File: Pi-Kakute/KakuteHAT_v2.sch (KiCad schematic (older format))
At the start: 51 parts, among them J1 40HAT, J12 FC_Socket, J2 Conn_01x02, J3 I2C, J4 Mout1_2, J5 Mout3_4, J6 RC_IN, J7 GPS2, J8 Power_Pad, J9 FC_Socket2, Q1 DMMT5401, Q2 DMG2305UX, SW1 Pi Power Switch, SW2 Pi Power Switch, U1 TPS22810, U2 AP2204RA-3.3, U3 KakuteF4_V2, U4 TPS54331DR, U5 NC7SZ00P5X, U6 CAT24C32

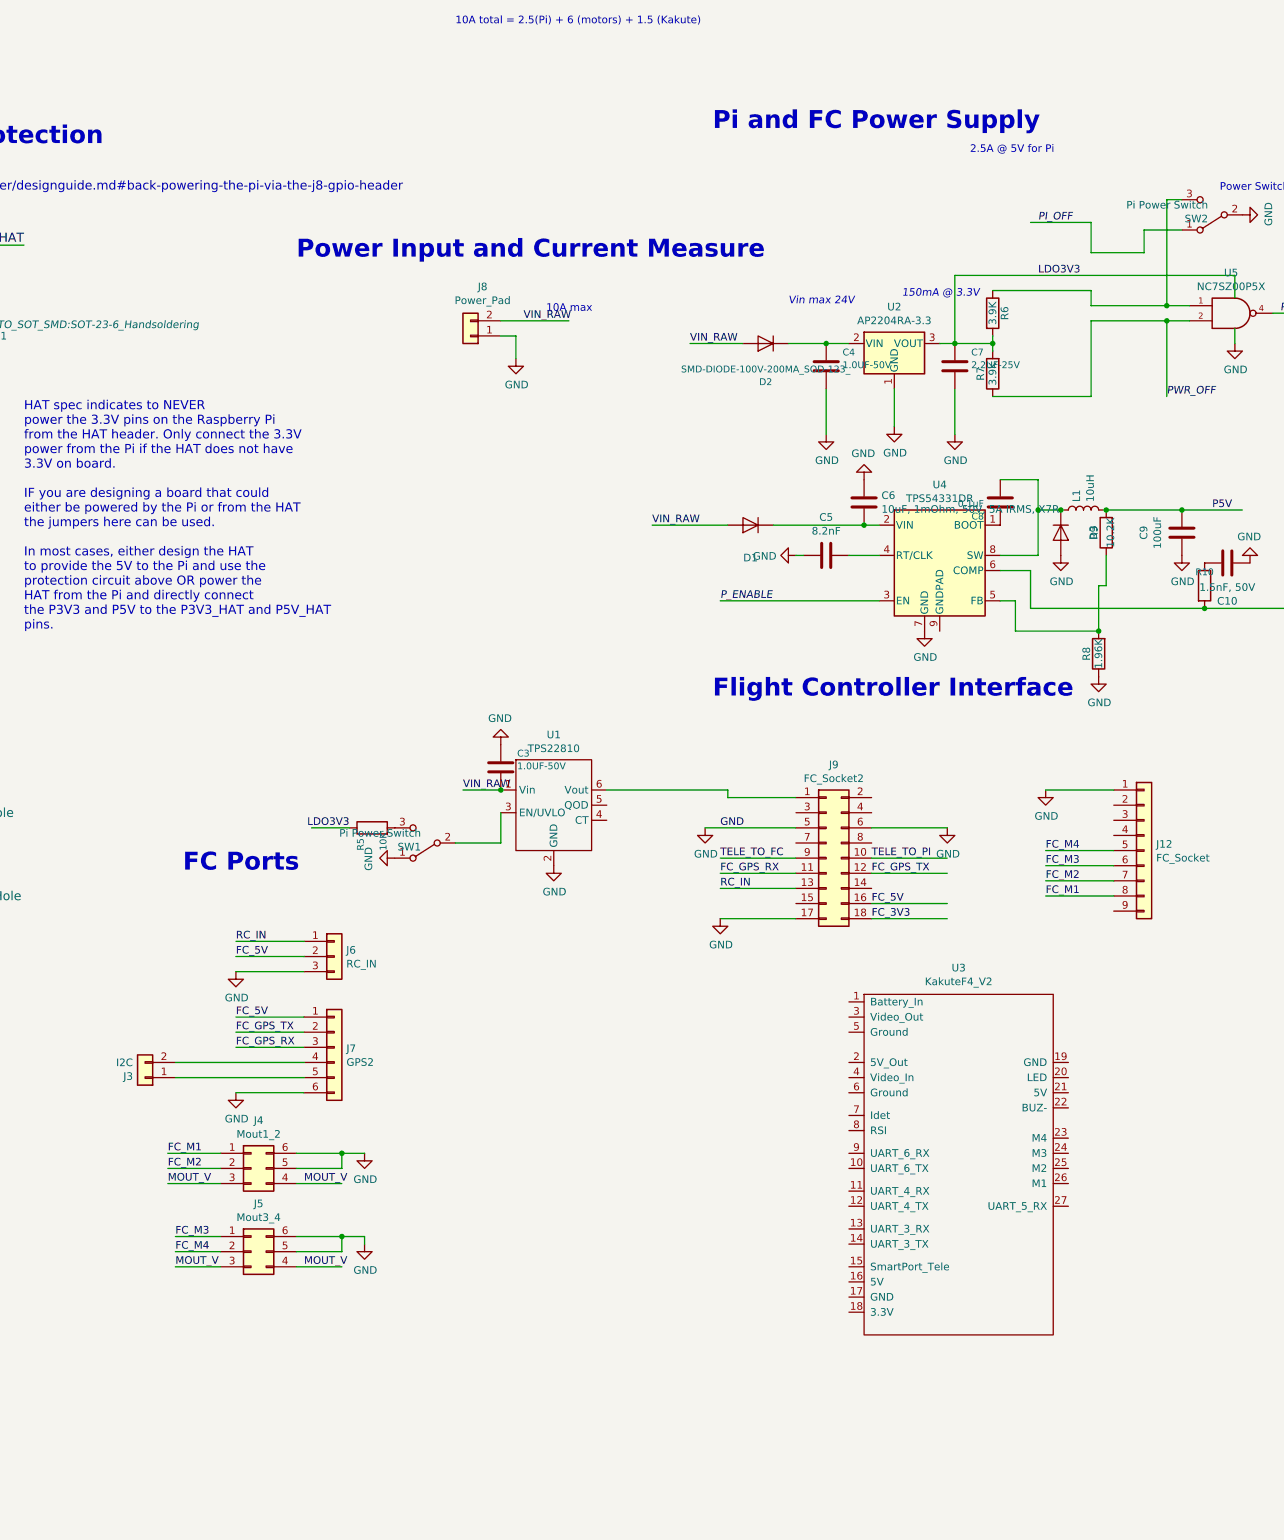
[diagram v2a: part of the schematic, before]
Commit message: Pi-Kakute: Updated power input to match Pi-Connect
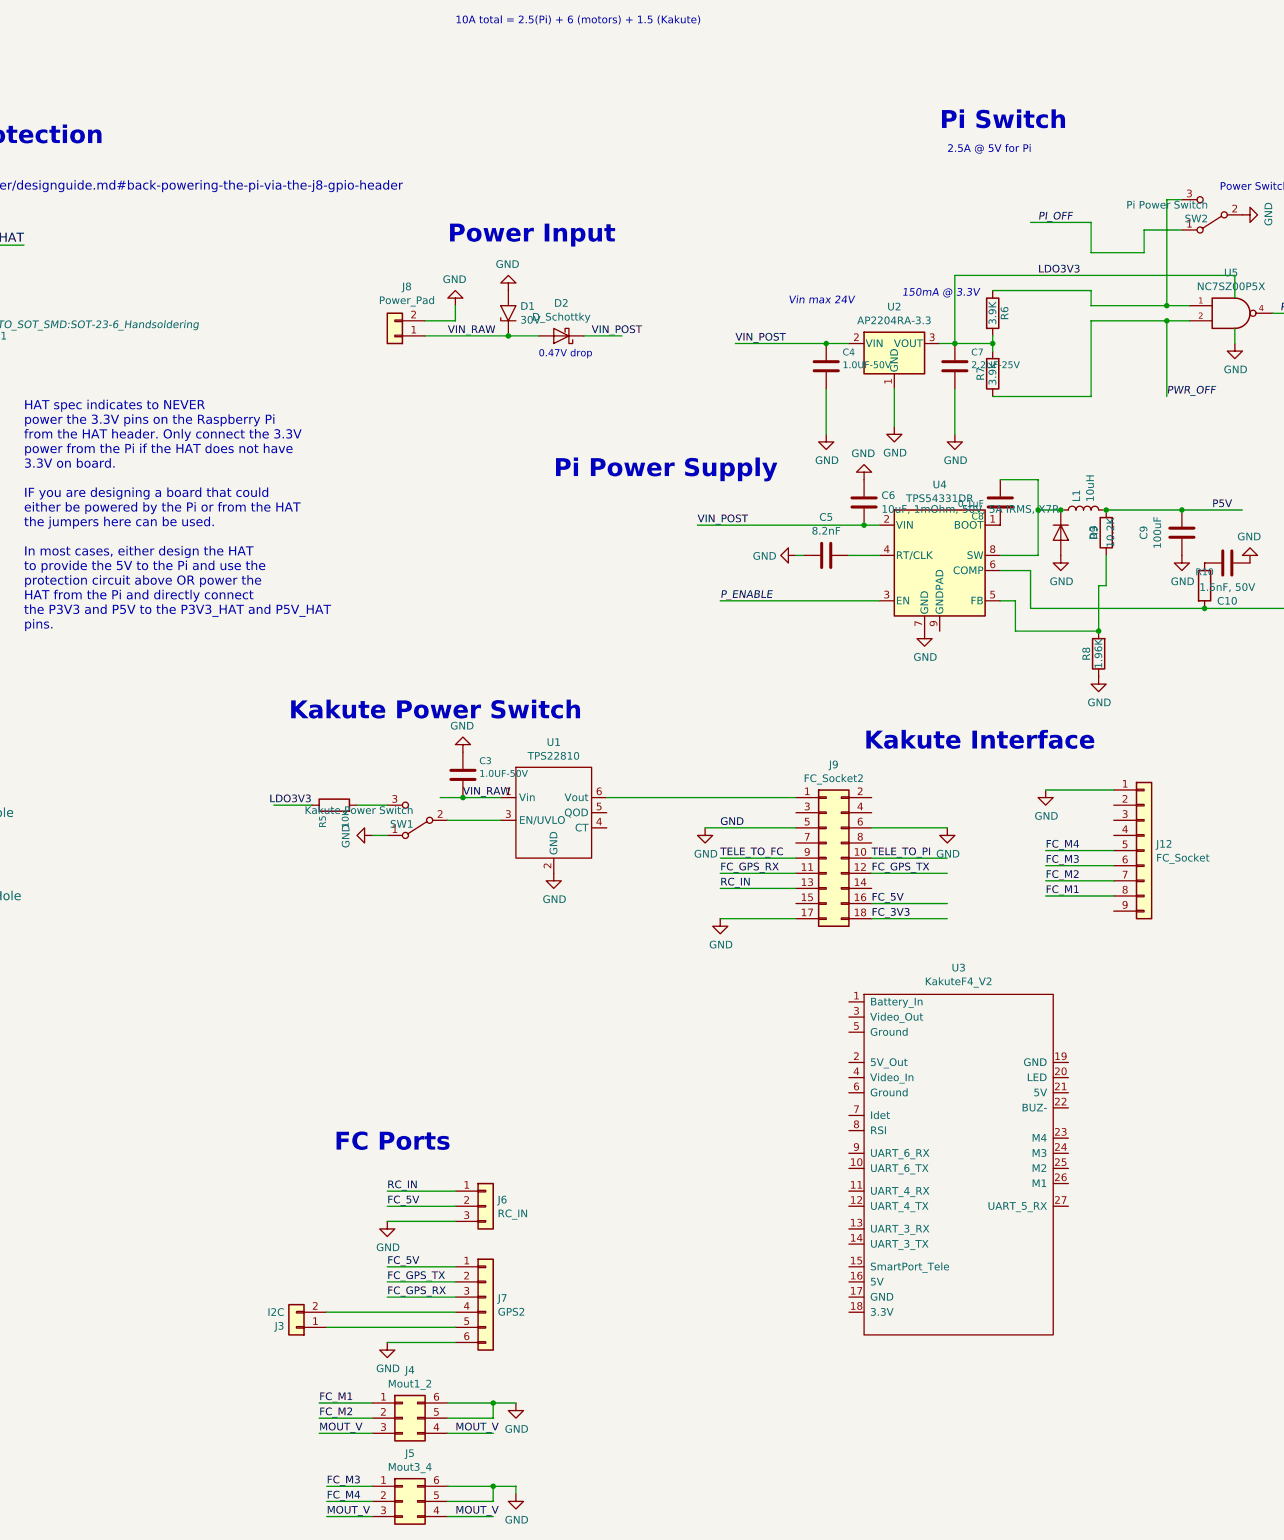
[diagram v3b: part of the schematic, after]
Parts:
- removed D1: PDS560-13, PowerDI:POWERDI5, symbol Device:D
- removed D2: SMD-DIODE-100V-200MA_SOD-123_, Diode_SMD:D_SOD-123, symbol Device:D
- added D1: 30V, Diode_SMD:D_SMA, symbol Diode:1.5KExxA
- added D2: D_Schottky, Diode_SMD:D_2010_5025Metric, symbol Device:D_Schottky
- J8: footprint Connector_Wire:SolderWirePad_1x02_P3.81mm_Drill1mm -> Connector_Molex:Molex_Nano-Fit_105313-xx02_1x02_P2.50mm_Horizontal; MFR (none) -> Molex; MPN (none) -> 1053131102; SPN (none) -> WM16893-ND; SPR (none) -> Digikey
- SW1: value Pi Power Switch -> Kakute Power Switch
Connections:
- net labels added: VIN_POST
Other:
- note added: "0.47V drop"
- note added: "Kakute Interface"
- note added: "Kakute Power Switch"
- note added: "Pi Power Supply"
- note added: "Pi Switch"
- note added: "Power Input"
- note removed: "10A max"
- note removed: "Flight Controller Interface"
- note removed: "Pi and FC Power Supply"
- note removed: "Power Input and Current Measure"
- moved on the sheet: C3, J3, J4, J5, J6, J7, J8, R5, SW1, U1

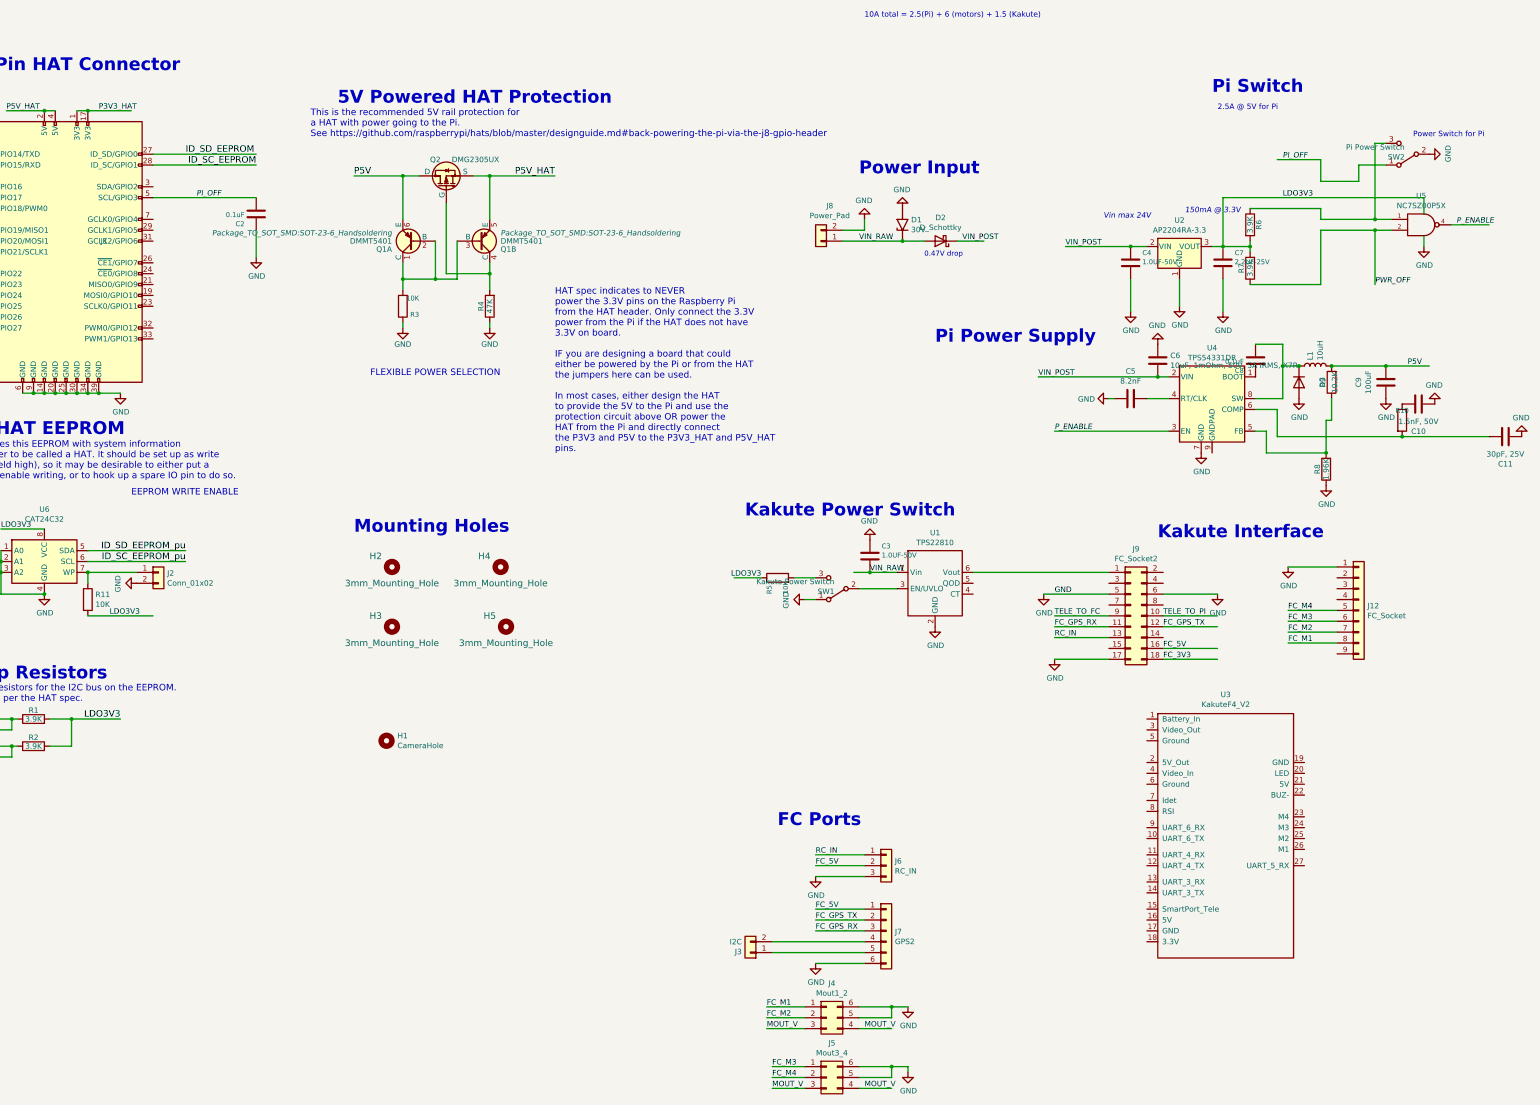
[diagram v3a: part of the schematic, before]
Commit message: Pi-Kakute: Upgraded 3.3 Reg and Fixed RC/Mout pins
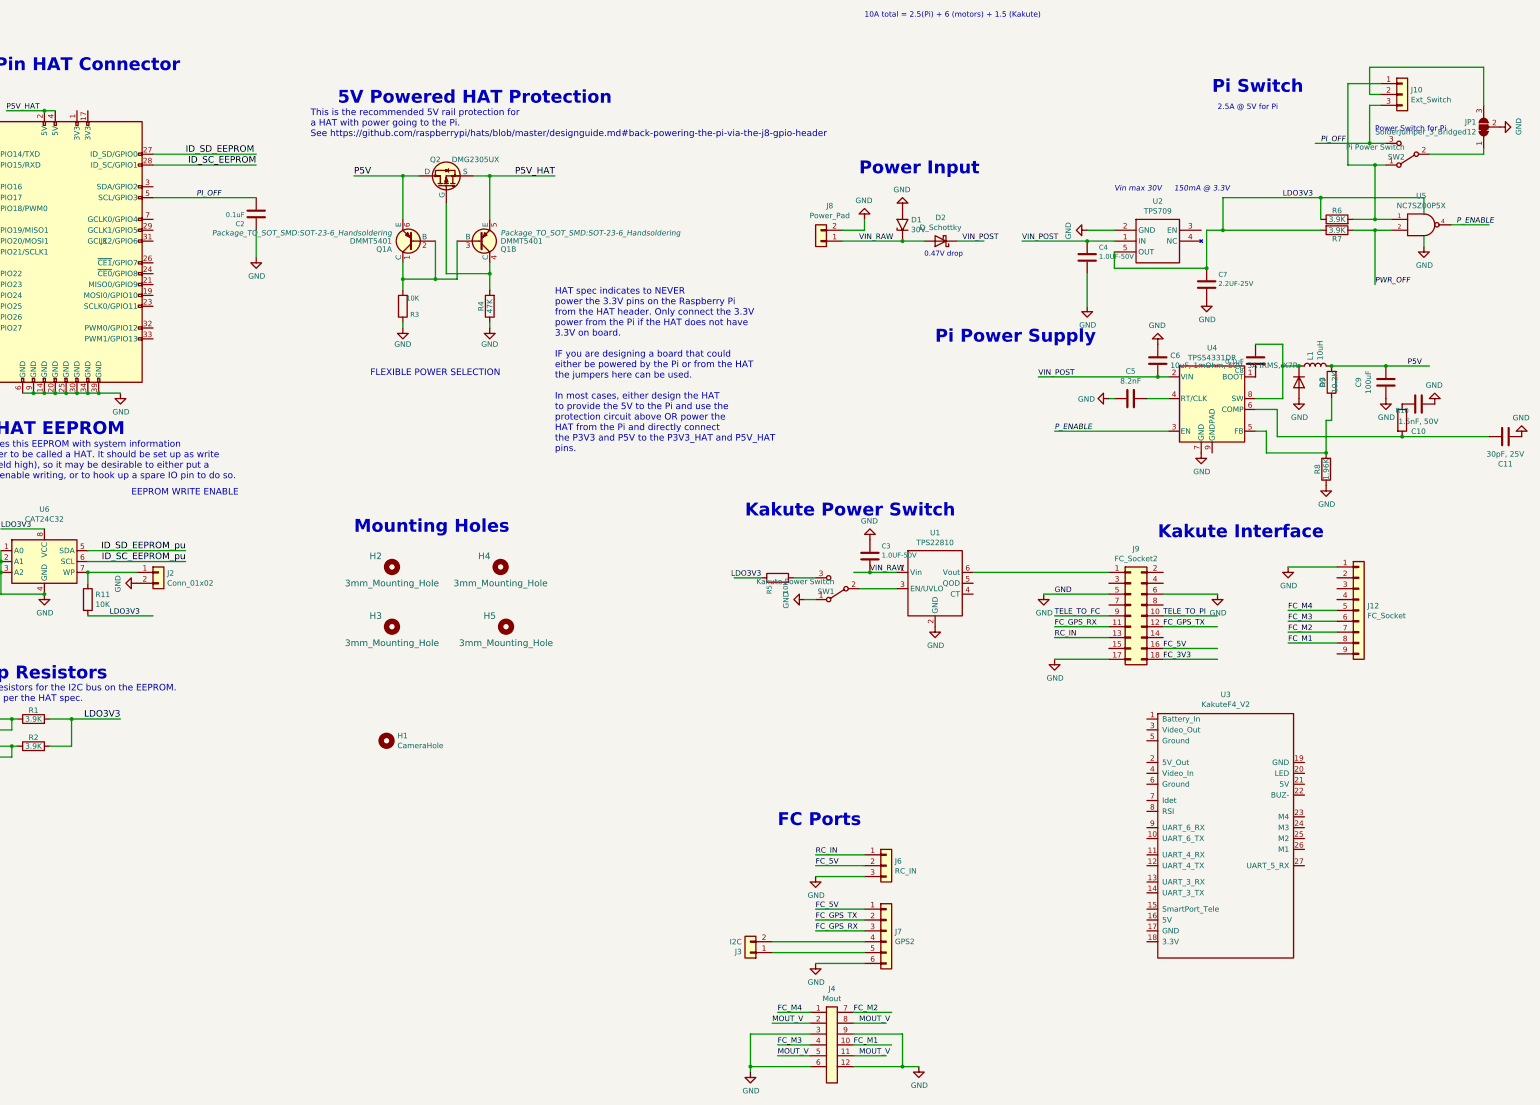
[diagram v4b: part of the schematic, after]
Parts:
- removed J4: Mout1_2, Connector_PinHeader_2.54mm:PinHeader_2x03_P2.54mm_Vertical, symbol Connector_Generic:Conn_02x03_Counter_Clockwise
- removed J5: Mout3_4, Connector_PinHeader_2.54mm:PinHeader_2x03_P2.54mm_Vertical, symbol Connector_Generic:Conn_02x03_Counter_Clockwise
- removed U2: AP2204RA-3.3, Package_TO_SOT_SMD:SOT-89-3, symbol Regulator_Linear:AP2204RA-3.3
- added J10: Ext_Switch, Connector_PinHeader_2.54mm:PinHeader_1x03_P2.54mm_Vertical, symbol Connector_Generic:Conn_01x03
- added J4: Mout, Kakute:PinHeader_4x03_P2.54mm_Horizontal, symbol Kakute:Conn_04x03
- added JP1: SolderJumper_3_Bridged12, Jumper:SolderJumper-3_P1.3mm_Bridged2Bar12_Pad1.0x1.5mm, symbol Jumper:SolderJumper_3_Bridged12
- added U2: TPS709, Package_TO_SOT_SMD:SOT-23-5_HandSoldering, symbol TI_additional:TPS709
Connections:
- net labels removed: P3V3_HAT
- wire segments 165 -> 168
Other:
- note added: "Vin max 30V"
- note removed: "Vin max 24V"
- moved on the sheet: C4, C7, R6, R7
